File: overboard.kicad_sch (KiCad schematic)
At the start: 192 parts, among them J1 USB_C_Receptacle_USB2.0, J2 Conn_01x04, J3 Trackpoint, J4 Conn_01x02, J5 Conn_01x02, J6 Conn_01x02, J7 Conn_01x02, K00 Key_Switch, K01 Key_Switch, K02 Key_Switch, K03 Key_Switch, K10 Key_Switch, K11 Key_Switch, K12 Key_Switch, K13 Key_Switch, K20 Key_Switch, K21 Key_Switch, K22 Key_Switch, K23 Key_Switch, K30 Key_Switch, K31 Key_Switch, K32 Key_Switch, K33 Key_Switch, K40 Key_Switch, K41 Key_Switch, K42 Key_Switch, K43 Key_Switch, K50 Key_Switch, K51 Key_Switch, K52 Key_Switch, K53 Key_Switch, K92 Key_Switch, K93 Key_Switch, K94 Key_Switch, Q1 Q_NPN_Darlington_BCE, Q2 Q_NPN_Darlington_BCE, Q3 Q_NMOS_DGS, SW1 Reset_SW, U1 Teensy2.0++

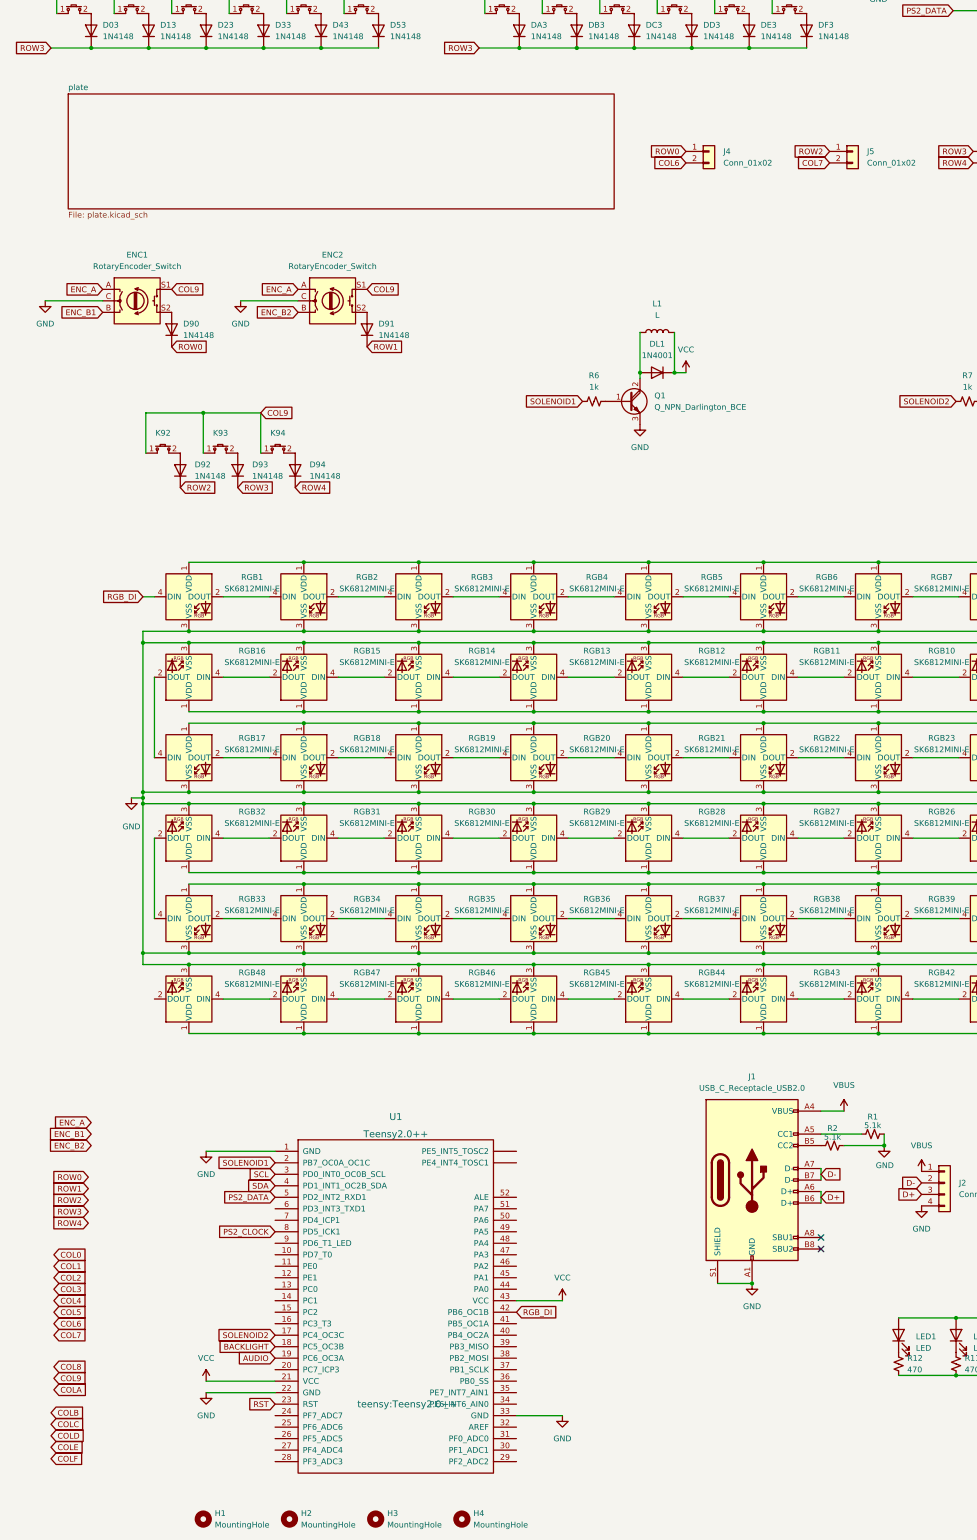
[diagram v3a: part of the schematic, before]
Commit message: Add plate, place RGB LEDs
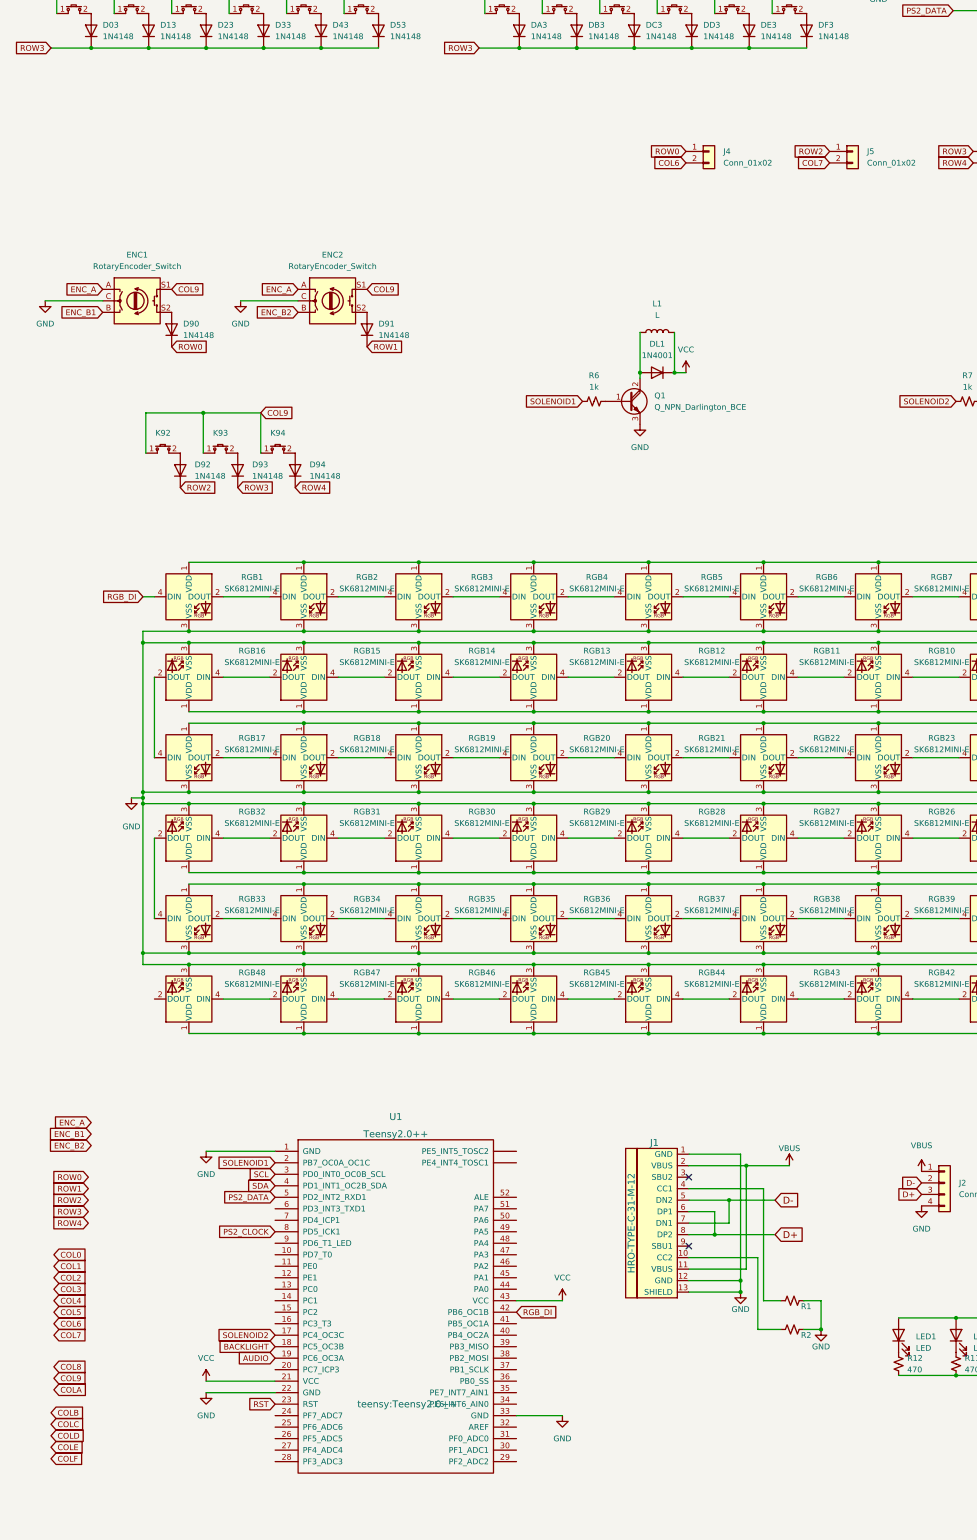
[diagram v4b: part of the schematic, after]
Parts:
- removed H1: MountingHole, User:GH60_Top_Left_Hole, symbol Mechanical:MountingHole
- removed H2: MountingHole, User:GH60_Top_Right_Hole, symbol Mechanical:MountingHole
- removed H3, H4: MountingHole, User:GH60_Side_Hole, symbol Mechanical:MountingHole
- removed J1: USB_C_Receptacle_USB2.0, USB_Type-C:USB_C_Receptacle_HRO_TYPE-C-31-M-12, symbol Connector:USB_C_Receptacle_USB2.0
- added J1: HRO-TYPE-C-31-M-12, symbol Type-C:HRO-TYPE-C-31-M-12
- R1, R2: value 5.1k -> (none); footprint Keebio-Parts:Resistor -> (none)
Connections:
- net D+: now also J1.6 (DP1), J1.8 (DP2)
- net D-: now also J1.5 (DN2), J1.7 (DN1)
- net GND: now also J1.1 (GND), J1.12 (GND), J1.13 (SHIELD)
- net VBUS: now also J1.11 (VBUS), J1.2 (VBUS)
- net at R2.2: now also J1.10 (CC2)
- net at R1.2: now also J1.4 (CC1)
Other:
- removed sheet plate

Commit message: Place components
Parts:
- removed J4, J5, J6, J7: Conn_01x02, Connector_PinHeader_2.54mm:PinHeader_1x02_P2.54mm_Vertical, symbol Connector_Generic:Conn_01x02
- added J4, J5: Conn_01x04, User:PinHeader_1x04_P2.54mm_Vertical_Centered, symbol Connector_Generic:Conn_01x04
- D00, D01, D02, D03, D10, D11, D12, D13, D20, D21, D22, D23, D30, D31, D32, D33, D40, D41, D42, D43, D50, D51, D52, D53, D90, D91, D92, D93, D94, DA0, DA1, DA2, DA3, DB0, DB1, DB2, DB3, DC0, DC1, DC2, DC3, DD0, DD1, DD2, DD3, DE0, DE1, DE2, DE3, DF0, DF1, DF2, DF3: footprint User:Diode_THT -> User:Diode_THT_P7.62mm
- J1: footprint (none) -> Type-C:HRO-TYPE-C-31-M-12-HandSoldering
- J2: footprint Connector_PinSocket_2.54mm:PinSocket_1x04_P2.54mm_Vertical -> Connector_PinHeader_2.54mm:PinHeader_1x04_P2.54mm_Horizontal
- J3: footprint Connector_PinHeader_2.54mm:PinHeader_1x05_P2.54mm_Vertical -> Connector_PinHeader_2.54mm:PinHeader_1x05_P2.54mm_Horizontal
- K00, K01, K02, K03, K10, K11, K12, K13, K20, K21, K22, K23, K30, K31, K32, K33, K40, K41, K42, K43, K50, K51, K52, K53, K92, K93, K94, KA0, KA1, KA2, KA3, KB0, KB1, KB2, KB3, KC0, KC1, KC2, KC3, KD0, KD1, KD2, KD3, KE0, KE1, KE2, KE3, KF0, KF1, KF2, KF3: footprint MK_Switches:MXOnly-1U-NoLED -> (none)
- L1, L2: footprint Connector_JST:JST_PH_S2B-PH-K_1x02_P2.00mm_Horizontal -> User:JST_PH_S2B-PH-K_1x02_P2.00mm_Horizontal
- LED1, LED2, LED3: footprint LED_THT:LED_D1.8mm_W3.3mm_H2.4mm -> User:LED_D1.8mm_W3.3mm_H2.4mm
- OLED1: footprint Display_0xLib:OLED_I2C_128x64_0.96inch -> User:128x64OLED
- Q1, Q2, Q3: footprint digikey-footprints:TO-220-3 -> User:TO-220-3
- R1, R2: value (none) -> 5.1k; footprint (none) -> User:Resistor_THT_P7.62mm
- R10: renamed from R12; footprint Keebio-Parts:Resistor -> User:Resistor_THT_P7.62mm
- R11, R3, R4, R5, R6, R7, R8, R9: footprint Keebio-Parts:Resistor -> User:Resistor_THT_P7.62mm
- R12: renamed from R10; footprint Keebio-Parts:Resistor -> User:Resistor_THT_P7.62mm
- U1: footprint teensy:Teensy2.0++ -> User:Teensy2.0++_43Pin
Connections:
- net COL6: now also J4.3 (Pin_3)
- net COL7: now also J4.4 (Pin_4)
- net COL8: now also J5.4 (Pin_4)
- net ROW0: now also J4.1 (Pin_1)
- net ROW1: now also J5.1 (Pin_1)
- net ROW2: now also J4.2 (Pin_2)
- net ROW3: now also J5.2 (Pin_2)
- net ROW4: now also J5.3 (Pin_3)

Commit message: Route PCB & plate
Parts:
- DL1, DL2: footprint Diode_THT:D_DO-41_SOD81_P7.62mm_Horizontal -> User:1N4001
- K00, K01, K02, K03, K10, K11, K12, K13, K20, K21, K22, K23, K30, K31, K32, K33, K40, K41, K42, K43, K50, K51, K52, K53, K92, K93, K94, KA0, KA1, KA2, KA3, KB0, KB1, KB2, KB3, KC0, KC1, KC2, KC3, KD0, KD1, KD2, KD3, KE0, KE1, KE2, KE3, KF0, KF1, KF2, KF3: footprint (none) -> User:MXOnly-1U
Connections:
- net COL0: now also U1.34 (PE6_INT6_AIN0)
- net COL1: now also U1.35 (PE7_INT7_AIN1)
- net COL2: now also U1.36 (PB0_SS)
- net COL3: now also U1.38 (PB2_MOSI)
- net COL4: now also U1.39 (PB3_MISO)
- net COL5: now also U1.40 (PB4_OC2A)
- net COL6: now also U1.12 (PE1)
- net COL7: now also U1.13 (PC0)
- net COL8: now also U1.20 (PC7_ICP3)
- net COL9: now also U1.11 (PE0)
- net COLA: now also U1.24 (PF7_ADC7)
- net COLB: now also U1.25 (PF6_ADC6)
- net COLC: now also U1.26 (PF5_ADC5)
- net COLD: now also U1.27 (PF4_ADC4)
- net COLE: now also U1.28 (PF3_ADC3)
- net COLF: now also U1.29 (PF2_ADC2)
- net ENC_A: now also U1.7 (PD4_ICP1)
- net ENC_B1: now also U1.6 (PD3_INT3_TXD1)
- net ENC_B2: now also U1.10 (PD7_T0)
- net ROW0: now also U1.14 (PC1)
- net ROW1: now also U1.15 (PC2)
- net ROW2: now also U1.37 (PB1_SCLK)
- net ROW3: now also U1.41 (PB5_OC1A)
- net ROW4: now also U1.16 (PC3_T3)
